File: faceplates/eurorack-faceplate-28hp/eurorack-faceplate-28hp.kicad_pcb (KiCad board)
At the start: 2 copper layers, 141.9 x 133.3 mm, 4 parts

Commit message: Moving mounting holes
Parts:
- moved REF** 2.42 mm to (5.08, 130.3)
- moved REF** 2.42 mm to (5.08, 3.00)
- moved REF** 2.32 mm to (136.8, 130.3)
- moved REF** 2.32 mm to (136.8, 3.00)
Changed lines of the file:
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@@
   (net 0 "")
   (footprint "MountingHole:MountingHole_3.2mm_M3" (layer "F.Cu")
-    (at 7.5 130.35)
+    (at 5.08 130.35)
     (descr "Mounting Hole 3.2mm, no annular, M3")
     (tags "mounting hole 3.2mm no annular m3")
@@
   )
   (footprint "MountingHole:MountingHole_3.2mm_M3" (layer "F.Cu")
-    (at 134.5 130.35)
+    (at 136.82 130.35)
     (descr "Mounting Hole 3.2mm, no annular, M3")
     (tags "mounting hole 3.2mm no annular m3")
@@
   )
   (footprint "MountingHole:MountingHole_3.2mm_M3" (layer "F.Cu")
-    (at 134.5 3)
+    (at 136.82 3)
     (descr "Mounting Hole 3.2mm, no annular, M3")
     (tags "mounting hole 3.2mm no annular m3")
@@
   )
   (footprint "MountingHole:MountingHole_3.2mm_M3" (layer "F.Cu")
-    (at 7.5 3)
+    (at 5.08 3)
     (descr "Mounting Hole 3.2mm, no annular, M3")
     (tags "mounting hole 3.2mm no annular m3")

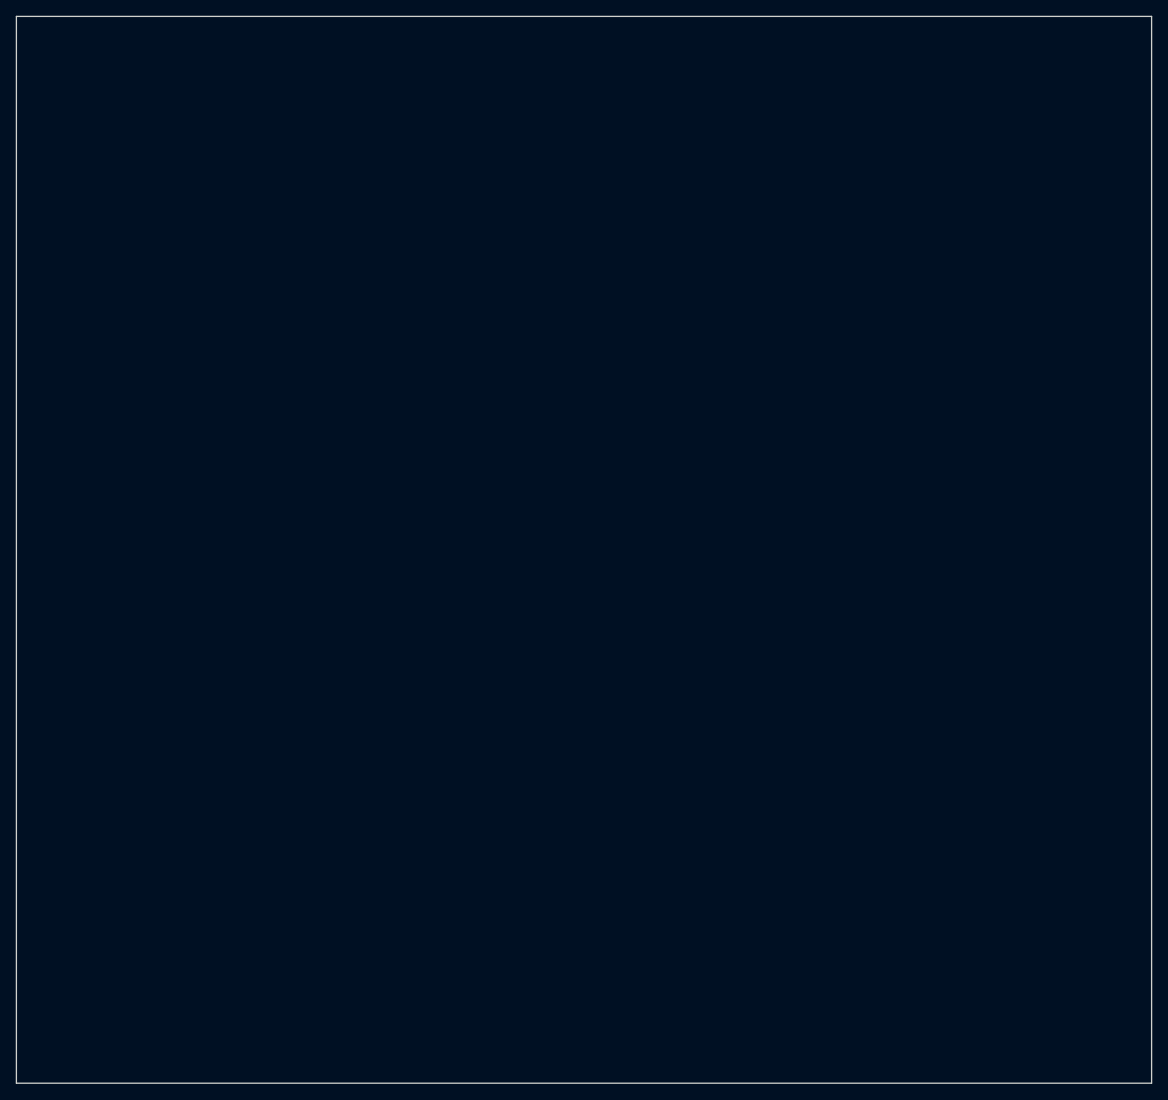
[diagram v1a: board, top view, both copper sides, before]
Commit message: Correcting panel height
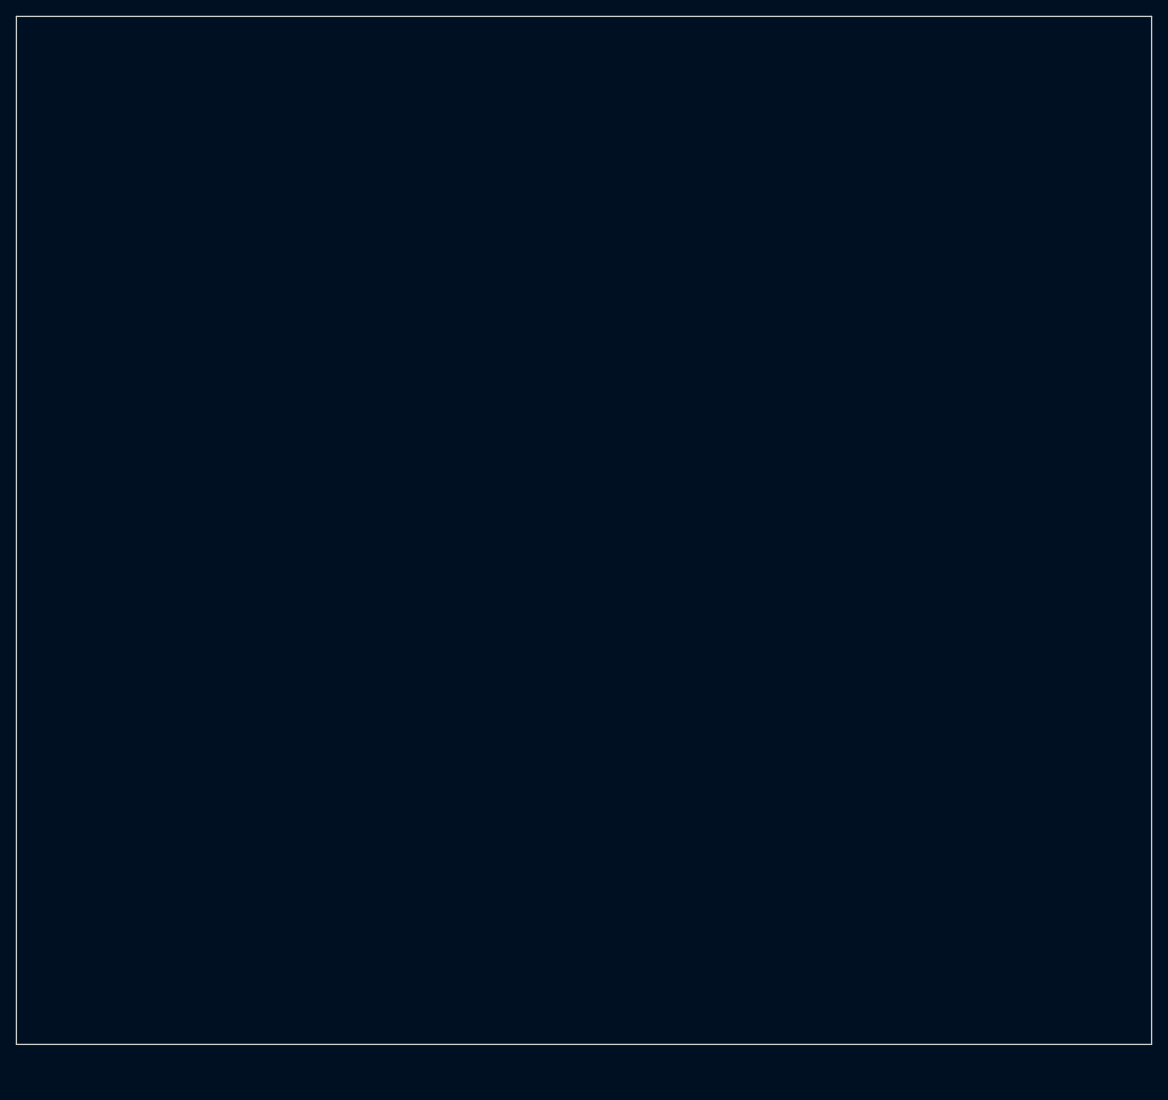
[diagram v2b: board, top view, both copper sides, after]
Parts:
- moved REF** 4.85 mm to (5.08, 125.5)
- moved REF** 4.85 mm to (136.8, 125.5)
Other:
- board size 141.9 x 133.3 mm -> 141.9 x 128.5 mm
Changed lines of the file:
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@@
   (net 0 "")
   (footprint "MountingHole:MountingHole_3.2mm_M3" (layer "F.Cu")
-    (at 5.08 130.35)
+    (at 5.08 125.5)
     (descr "Mounting Hole 3.2mm, no annular, M3")
     (tags "mounting hole 3.2mm no annular m3")
@@
   )
   (footprint "MountingHole:MountingHole_3.2mm_M3" (layer "F.Cu")
-    (at 136.82 130.35)
+    (at 136.82 125.5)
     (descr "Mounting Hole 3.2mm, no annular, M3")
     (tags "mounting hole 3.2mm no annular m3")
@@
     (pad "" np_thru_hole oval locked (at 0 0) (size 7 3.2) (drill oval 7 3.2) (layers F&B.Cu *.Mask))
   )
-  (gr_line (start 141.9 0) (end 141.9 133.35) (layer "Edge.Cuts") (width 0.1))
-  (gr_line (start 0 133.35) (end 0 0) (layer "Edge.Cuts") (width 0.1))
+  (gr_line (start 141.9 0) (end 141.9 128.5) (layer "Edge.Cuts") (width 0.1))
+  (gr_line (start 0 128.5) (end 0 0) (layer "Edge.Cuts") (width 0.1))
   (gr_line (start 0 0) (end 141.9 0) (layer "Edge.Cuts") (width 0.1))
-  (gr_line (start 141.9 133.35) (end 0 133.35) (layer "Edge.Cuts") (width 0.1))
+  (gr_line (start 141.9 128.5) (end 0 128.5) (layer "Edge.Cuts") (width 0.1))
 )
